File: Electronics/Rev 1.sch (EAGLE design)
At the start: 211 parts, among them P1 5-2301994-4, Q1 BCV27, Q10 BCV26SOT23, Q11 BCV27, Q12 BCV26SOT23, Q13 BCV27, Q14 BCV26SOT23, Q15 BCV27, Q16 BCV26SOT23, Q17 BCV27, Q18 BCV26SOT23, Q19 BCV27, Q2 BCV26SOT23, Q20 BCV26SOT23, Q21 BCV27, Q22 BCV26SOT23, Q23 BCV27, Q24 BCV26SOT23, Q25 PBSS4360XFPBSS4360XF, Q26 MMBT3904,215MMBT3904,215, Q27 PBSS4360XFPBSS4360XF, Q28 MMBT3904,215MMBT3904,215, Q29 PBSS4360XFPBSS4360XF, Q3 BCV27, Q30 TIP35CTIP35C, Q31 PBSS4360XFPBSS4360XF, Q32 MMBT3904,215MMBT3904,215, Q33 TIP35CTIP35C, Q34 PBSS4360XFPBSS4360XF, Q35 MMBT3904,215MMBT3904,215, Q36 MMBT3904,215MMBT3904,215, Q37 MMBT3904,215MMBT3904,215, Q38 MMBT3904,215MMBT3904,215, Q39 MMBT3904,215MMBT3904,215, Q4 BCV26SOT23, Q5 BCV27, Q6 BCV26SOT23, Q7 BCV27, Q8 BCV26SOT23, Q9 BCV27, U1 LFXP6E-3FN256C, U10 RPI, U11 3.3V, U12 3.3V, U13 3.3V, U14 LT1025CN8PBF, U15 LTC1049CS8#PBF, U16 MCP3021A1T-E/OTSOT23, U2 MCP4251, U3 MCP4251, U4 MMA8453QR116QFN, U5 74AHC1G66GW,125TSSOP6, U6 74AHC1G66GW,125TSSOP6, U7 74AHC1G66GW,125TSSOP6, U8 MCP3021A1T-E/OTSOT23, U9 MC74HC164BDR2GMC74HC164BDR2G, Y1 DSC1122B

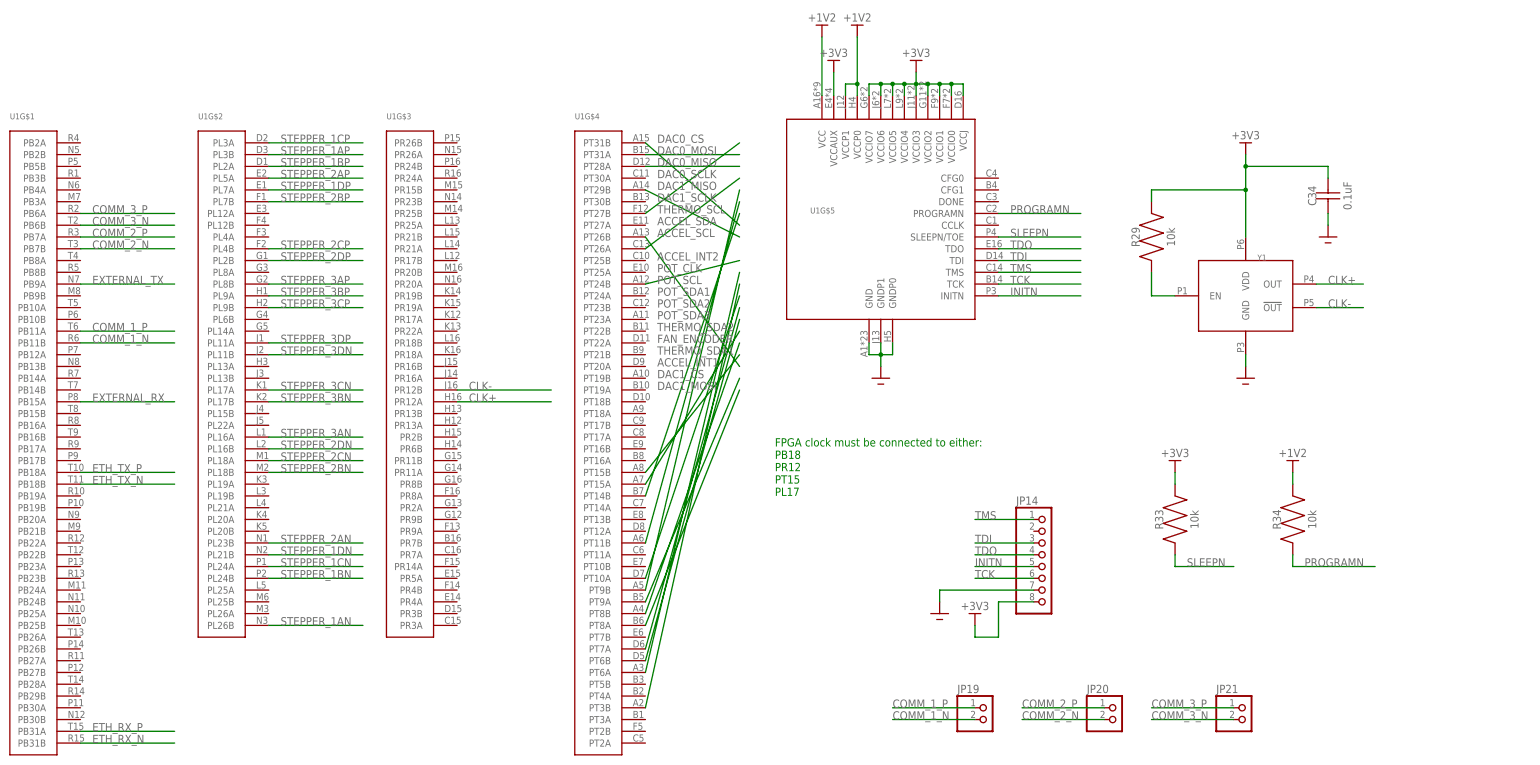
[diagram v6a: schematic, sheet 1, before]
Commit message: Added GPIO pins
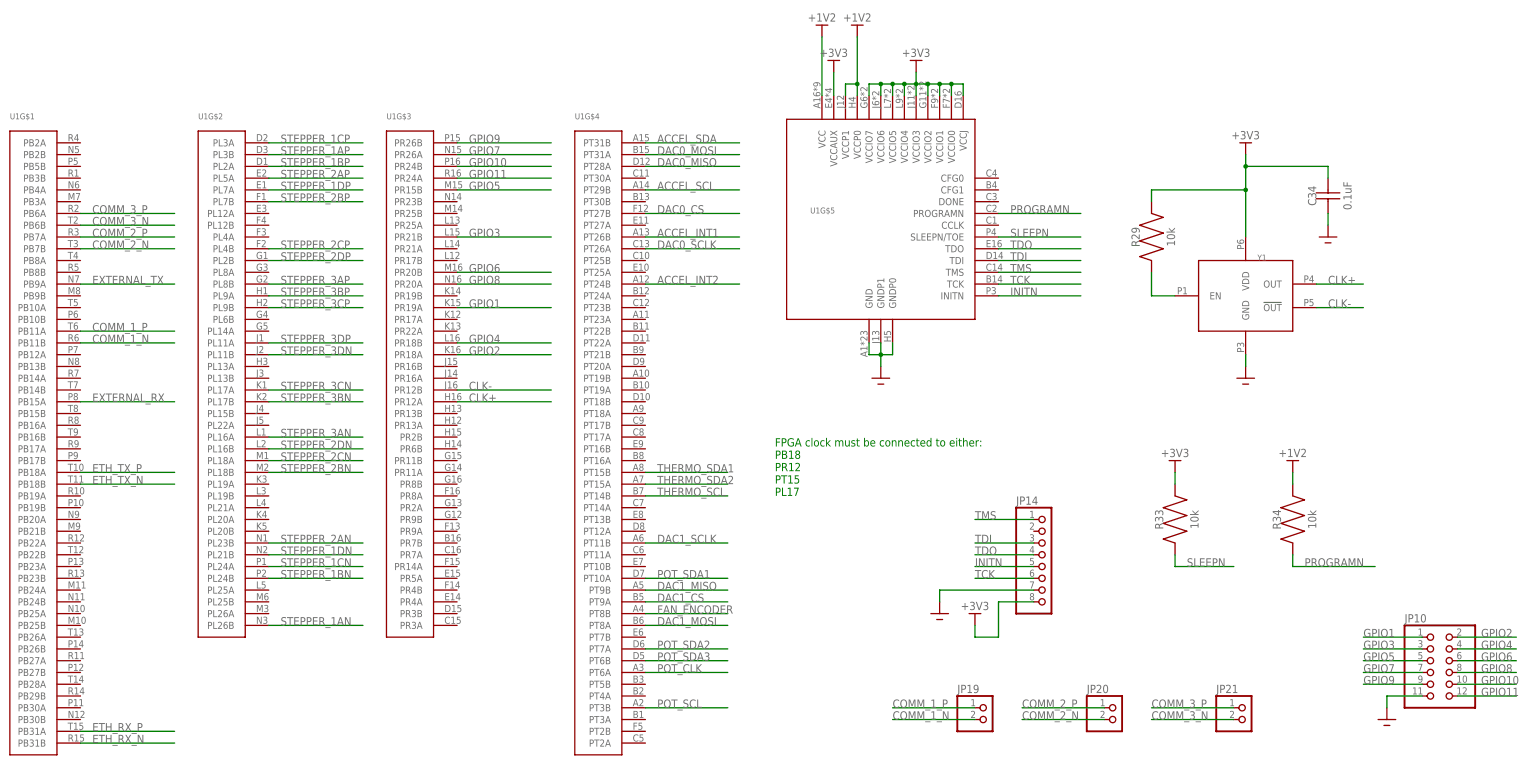
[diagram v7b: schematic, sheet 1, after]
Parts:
- added JP10: (no value), fillament-winder:PINHD-2X6
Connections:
- new net GPIO1: JP10.1, U1G$3.PR19A
- new net GPIO10: JP10.10, U1G$3.PR24B
- new net GPIO11: JP10.12, U1G$3.PR24A
- new net GPIO2: JP10.2, U1G$3.PR18A
- new net GPIO3: JP10.3, U1G$3.PR21B
- new net GPIO4: JP10.4, U1G$3.PR18B
- new net GPIO5: JP10.5, U1G$3.PR15B
- new net GPIO6: JP10.6, U1G$3.PR20B
- new net GPIO7: JP10.7, U1G$3.PR26A
- new net GPIO8: JP10.8, U1G$3.PR20A
- new net GPIO9: JP10.9, U1G$3.PR26B
- net GND: now also JP10.11
